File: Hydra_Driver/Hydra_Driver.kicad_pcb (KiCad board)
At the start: 2 copper layers, 58 x 42 mm, 99 parts, among them IC101 ESP32-S3-WROOM-1-N4, IC201 DRV8313RHHR, IC301 DRV8313RHHR, J101 USB4105-GF-A, J102 Conn_01x02, J103 Conn_01x06, J104 Conn_01x04, J105 Conn_01x03, J106 Conn_01x06, J107 Conn_01x04, J108 Conn_01x03, J109 Conn_01x02, SW101 SW_SPST, SW102 SW_SPST, U101 USBLC6-2SC6, U102 MIC5504-3.3YM5-TR, U103 SN74LVC1G80DBVR, U201 INA4181A2IPWR, U301 INA4181A2IPWR

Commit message: Fixed SPI daisy chain issue
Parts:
- removed J106: Conn_01x06, Connector_PinHeader_2.54mm:PinHeader_1x06_P2.54mm_Horizontal
- added J110: Conn_01x07, Connector_PinHeader_2.54mm:PinHeader_1x07_P2.54mm_Horizontal, B.Cu at (27.8, 7.25)
- IC101: footprint Touchstone:ESP32S3WROOM1N4 -> Touchscape:ESP32S3WROOM1N4
- IC201, IC301: footprint Touchstone:QFN50P600X600X100-37N-D -> Touchscape:QFN50P600X600X100-37N-D
- J101: footprint Touchstone:GCT_USB4105-GF-A -> Touchscape:GCT_USB4105-GF-A
- J102, J109: footprint Touchstone:AMASS_XT30U-F_1x02_P5.0mm_Vertical -> Touchscape:AMASS_XT30U-F_1x02_P5.0mm_Vertical
- J103: value Conn_01x06 -> Conn_01x07; footprint Connector_PinSocket_2.54mm:PinSocket_1x06_P2.54mm_Horizontal -> Connector_PinSocket_2.54mm:PinSocket_1x07_P2.54mm_Horizontal
- J104, J107: footprint Touchstone:CONN_CCSH-W10R-04TR-BK-A_ADA -> Touchscape:CONN_CCSH-W10R-04TR-BK-A_ADA
- SW101, SW102: footprint Touchstone:SW_B3U-1000P -> Touchscape:SW_B3U-1000P
- U102: footprint Touchstone:SOT-23-5_MC_MCH -> Touchscape:SOT-23-5_MC_MCH
- U103: footprint Touchstone:DBV5 -> Touchscape:DBV5
- U201, U301: footprint Touchstone:PW20_TEX -> Touchscape:PW20_TEX
- moved J103 0.55 mm to (27.8, 35.0)
- moved R110 0.40 mm to (28.0, 32.1)
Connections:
- IC101 pad 8: /CSOUT -> /CSIN
- J103 pad 4: /MOSI -> /MISO
- J103 pad 5: GND -> /MOSI
- J103 pad 6: +5V -> GND
- R110 pad 2: /CSOUT -> /CSIN
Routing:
- net +3.3V: track 219.1 -> 161.3 mm
- net /MISO: track 24.4 -> 51.6 mm
- net /MOSI: track 30.2 -> 56.7 mm
- net /CSIN: track 5.74 -> 17.8 mm
- net /CSOUT: track 51.6 -> 49.5 mm, vias 2 -> 1
- net /D+: track 36.5 -> 35.6 mm
- net /D-: track 35.8 -> 35.0 mm

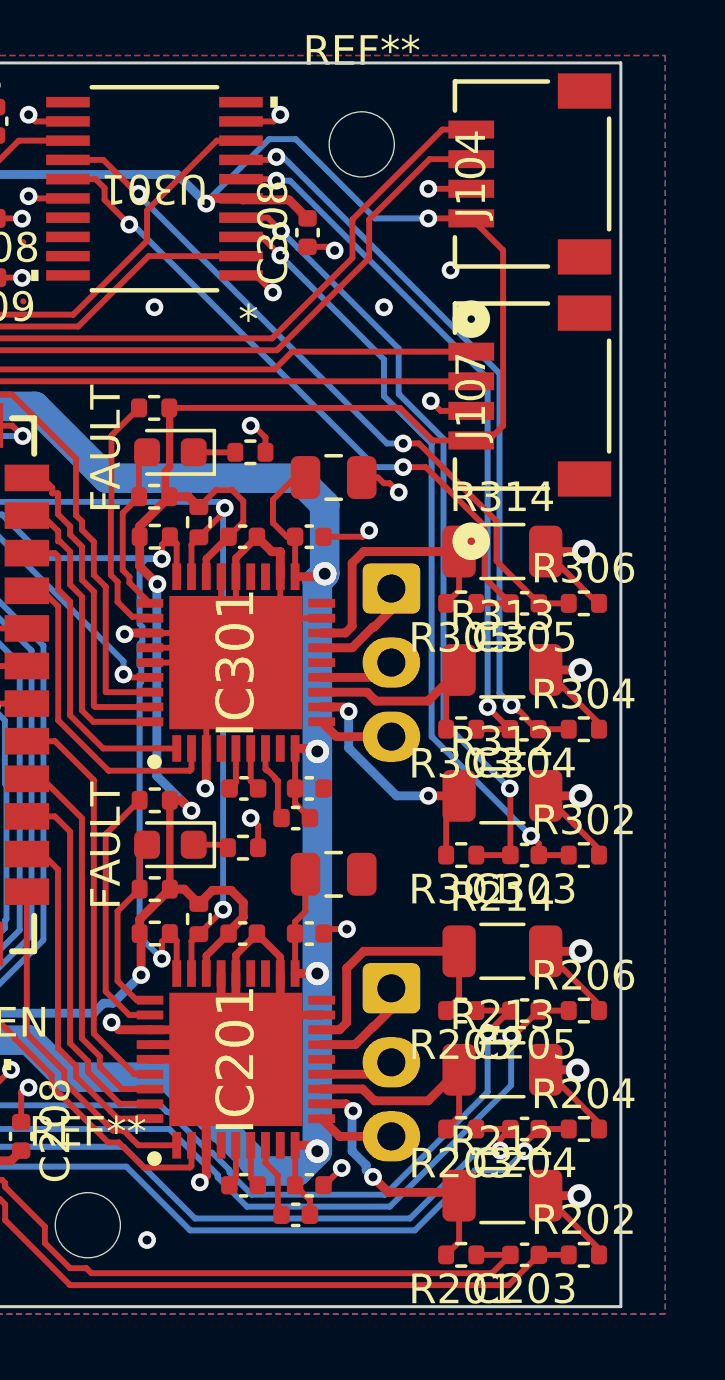
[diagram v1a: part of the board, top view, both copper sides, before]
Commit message: Fixed Kelvin connections and filter circuits
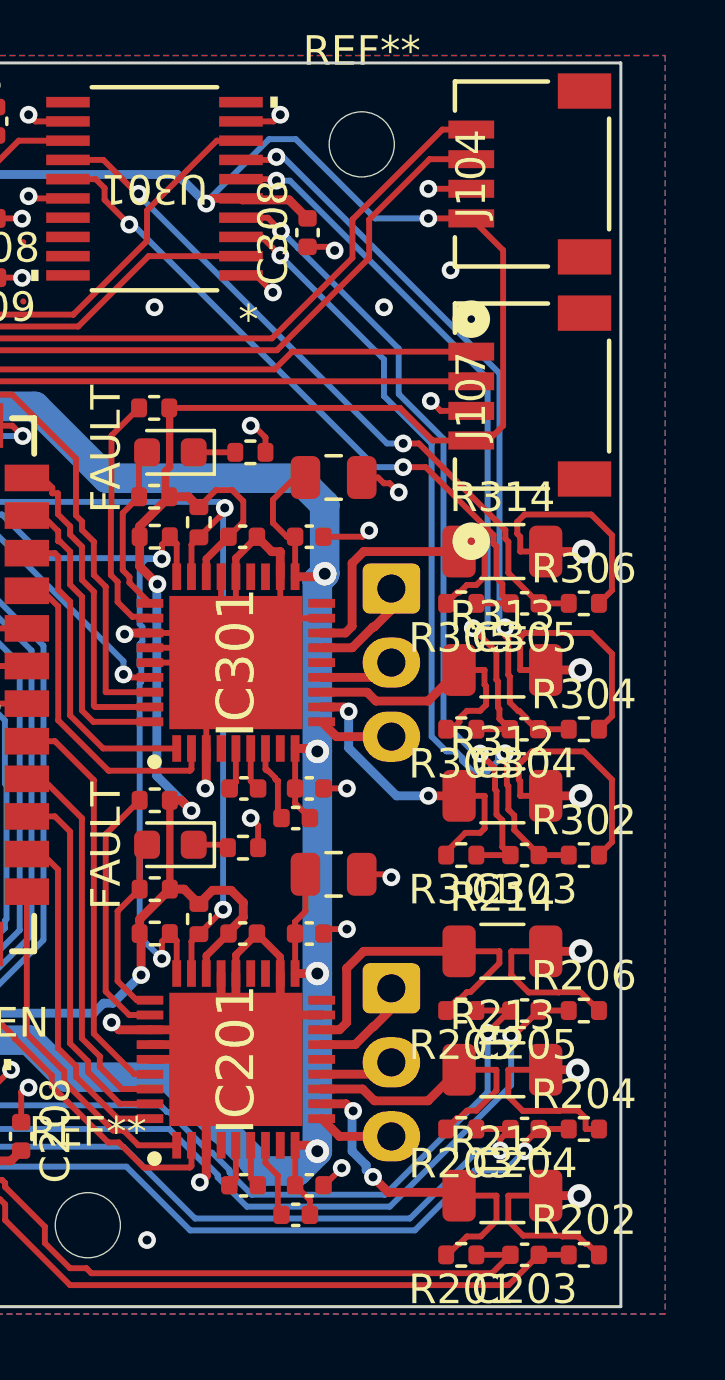
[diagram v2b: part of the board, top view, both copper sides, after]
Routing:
- net GND: track 139.9 -> 167.0 mm, vias 63 -> 65
- net /Driver_Unit/SGND1: track 9.05 -> 11.2 mm
- net /Driver_Unit/SGND3: track 8.99 -> 11.0 mm
- net /Driver_Unit/SGND2: track 7.42 -> 9.44 mm
- net /Driver_Unit1/IN-1: track 26.5 -> 28.4 mm
- net /Driver_Unit1/SGND2: track 7.38 -> 9.01 mm
- net /Driver_Unit1/SGND1: track 8.78 -> 10.3 mm
- net /Driver_Unit1/SGND3: track 8.96 -> 10.4 mm
- net /Driver_Unit1/IN+2: track 24.4 -> 25.0 mm
